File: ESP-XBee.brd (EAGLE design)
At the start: 10 parts, among them SW1 434111043826

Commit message: seeedstudio GERBER generated
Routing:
- net N$2: track 109.9 -> 0.00 mm
- net RESET: track 45.6 -> 47.1 mm, vias 3 -> 2
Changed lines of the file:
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@@
 </class>
 </classes>
-<designrules name="default">
+<designrules name="SeeedStudio_2layer_DRU_no_angle_20140221">
 <description language="de">&lt;b&gt;EAGLE Design Rules&lt;/b&gt;
 &lt;p&gt;
@@
 necessary adjustments and save your customized
 design rules under a new name.</description>
+<description language="zh">&lt;b&gt;Seeed Studio EAGLE Design Rules&lt;/b&gt;
+</description>
 <param name="layerSetup" value="(1*16)"/>
-<param name="mtCopper" value="0.035mm 0.035mm 0.035mm 0.035mm 0.035mm 0.035mm 0.035mm 0.035mm 0.035mm 0.035mm 0.035mm 0.035mm 0.035mm 0.035mm 0.035mm 0.035mm"/>
-<param name="mtIsolate" value="1.5mm 0.15mm 0.2mm 0.15mm 0.2mm 0.15mm 0.2mm 0.15mm 0.2mm 0.15mm 0.2mm 0.15mm 0.2mm 0.15mm 0.2mm"/>
-<param name="mdWireWire" value="8mil"/>
-<param name="mdWirePad" value="8mil"/>
-<param name="mdWireVia" value="8mil"/>
-<param name="mdPadPad" value="8mil"/>
-<param name="mdPadVia" value="8mil"/>
-<param name="mdViaVia" value="8mil"/>
-<param name="mdSmdPad" value="8mil"/>
-<param name="mdSmdVia" value="8mil"/>
-<param name="mdSmdSmd" value="8mil"/>
+<param name="mtCopper" value="0.035mm 0.0175mm 0.035mm 0.035mm 0.035mm 0.035mm 0.035mm 0.035mm 0.035mm 0.035mm 0.035mm 0.035mm 0.035mm 0.035mm 0.0175mm 0.035mm"/>
+<param name="mtIsolate" value="1.5mm 1.1mm 0.2mm 0.15mm 0.2mm 0.15mm 0.2mm 0.15mm 0.2mm 0.15mm 0.2mm 0.15mm 0.2mm 0.15mm 0.2mm"/>
+<param name="mdWireWire" value="6mil"/>
+<param name="mdWirePad" value="6mil"/>
+<param name="mdWireVia" value="6mil"/>
+<param name="mdPadPad" value="6mil"/>
+<param name="mdPadVia" value="6mil"/>
+<param name="mdViaVia" value="6mil"/>
+<param name="mdSmdPad" value="0mil"/>
+<param name="mdSmdVia" value="0mil"/>
+<param name="mdSmdSmd" value="0mil"/>
 <param name="mdViaViaSameLayer" value="8mil"/>
 <param name="mnLayersViaInSmd" value="2"/>
-<param name="mdCopperDimension" value="40mil"/>
-<param name="mdDrill" value="8mil"/>
+<param name="mdCopperDimension" value="10mil"/>
+<param name="mdDrill" value="10mil"/>
 <param name="mdSmdStop" value="0mil"/>
-<param name="msWidth" value="10mil"/>
-<param name="msDrill" value="24mil"/>
-<param name="msMicroVia" value="9.99mm"/>
+<param name="msWidth" value="6mil"/>
+<param name="msDrill" value="12mil"/>
+<param name="msMicroVia" value="12mil"/>
 <param name="msBlindViaRatio" value="0.5"/>
 <param name="rvPadTop" value="0.25"/>
@@
 <param name="rlMinPadBottom" value="10mil"/>
 <param name="rlMaxPadBottom" value="20mil"/>
-<param name="rlMinViaOuter" value="8mil"/>
+<param name="rlMinViaOuter" value="6mil"/>
 <param name="rlMaxViaOuter" value="20mil"/>
-<param name="rlMinViaInner" value="8mil"/>
+<param name="rlMinViaInner" value="6mil"/>
 <param name="rlMaxViaInner" value="20mil"/>
 <param name="rlMinMicroViaOuter" value="4mil"/>
@@
 <param name="psTop" value="-1"/>
 <param name="psBottom" value="-1"/>
-<param name="psFirst" value="-1"/>
+<param name="psFirst" value="0"/>
 <param name="psElongationLong" value="100"/>
 <param name="psElongationOffset" value="100"/>
 <param name="mvStopFrame" value="1"/>
 <param name="mvCreamFrame" value="0"/>
-<param name="mlMinStopFrame" value="4mil"/>
-<param name="mlMaxStopFrame" value="4mil"/>
+<param name="mlMinStopFrame" value="2mil"/>
+<param name="mlMaxStopFrame" value="2mil"/>
 <param name="mlMinCreamFrame" value="0mil"/>
 <param name="mlMaxCreamFrame" value="0mil"/>
-<param name="mlViaStopLimit" value="0mil"/>
+<param name="mlViaStopLimit" value="100mil"/>
 <param name="srRoundness" value="0"/>
 <param name="srMinRoundness" value="0mil"/>
@@
 <param name="checkAngle" value="0"/>
 <param name="checkFont" value="1"/>
-<param name="checkRestrict" value="1"/>
+<param name="checkRestrict" value="0"/>
 <param name="useDiameter" value="13"/>
 <param name="maxErrors" value="50"/>
@@
 <contactref element="C2" pad="1"/>
 <contactref element="R5" pad="2"/>
-<wire x1="34.417" y1="42.543" x2="36.197" y2="42.543" width="0.3048" layer="1"/>
-<wire x1="36.197" y1="42.543" x2="36.83" y2="41.91" width="0.3048" layer="1"/>
-<via x="36.83" y="41.91" extent="1-16" drill="0.6" shape="octagon"/>
-<wire x1="36.83" y1="41.91" x2="36.83" y2="40.64" width="0.3048" layer="16"/>
-<wire x1="36.83" y1="40.64" x2="36.195" y2="40.005" width="0.3048" layer="16"/>
-<wire x1="36.195" y1="40.005" x2="34.798" y2="40.005" width="0.3048" layer="16"/>
-<wire x1="34.798" y1="40.005" x2="34.417" y2="39.624" width="0.3048" layer="16"/>
-<wire x1="34.417" y1="39.624" x2="34.417" y2="38.481" width="0.3048" layer="16"/>
-<wire x1="34.417" y1="38.481" x2="33.274" y2="37.338" width="0.3048" layer="16"/>
-<wire x1="33.274" y1="37.338" x2="31.607" y2="37.338" width="0.3048" layer="16"/>
-<wire x1="31.607" y1="37.338" x2="31.545" y2="37.4" width="0.3048" layer="16"/>
 <wire x1="42.407" y1="22.225" x2="42.407" y2="23.357" width="0.3048" layer="1"/>
 <wire x1="42.407" y1="23.357" x2="43.18" y2="24.13" width="0.3048" layer="1"/>
@@
 <wire x1="46.101" y1="32.131" x2="45.201" y2="32.131" width="0.3048" layer="16"/>
 <wire x1="45.201" y1="32.131" x2="44.958" y2="31.38" width="0.3048" layer="16"/>
-<wire x1="36.83" y1="40.64" x2="36.83" y2="40.513" width="0.3048" layer="16"/>
-<wire x1="36.83" y1="40.513" x2="39.243" y2="36.83" width="0.3048" layer="16"/>
-<via x="39.243" y="36.83" extent="1-16" drill="0.6" shape="octagon"/>
-<wire x1="39.243" y1="36.83" x2="43.688" y2="36.83" width="0.3048" layer="1"/>
 <wire x1="43.688" y1="36.83" x2="46.101" y2="34.417" width="0.3048" layer="1"/>
 <wire x1="46.101" y1="34.417" x2="46.101" y2="32.131" width="0.3048" layer="1"/>
+<wire x1="43.688" y1="36.83" x2="40.005" y2="36.83" width="0.3048" layer="1"/>
+<wire x1="40.005" y1="36.83" x2="39.243" y2="37.592" width="0.3048" layer="1"/>
+<wire x1="39.243" y1="37.592" x2="39.243" y2="40.64" width="0.3048" layer="1"/>
+<wire x1="31.545" y1="37.4" x2="32.955" y2="37.4" width="0.3048" layer="16"/>
+<wire x1="32.955" y1="37.4" x2="36.83" y2="41.275" width="0.3048" layer="16"/>
+<wire x1="34.542" y1="42.418" x2="34.417" y2="42.543" width="0.3048" layer="1"/>
+<wire x1="36.83" y1="41.275" x2="36.83" y2="42.545" width="0.3048" layer="16"/>
+<via x="36.83" y="42.545" extent="1-16" drill="0.6" shape="octagon"/>
+<wire x1="36.83" y1="42.545" x2="34.419" y2="42.545" width="0.3048" layer="1"/>
+<wire x1="34.419" y1="42.545" x2="34.417" y2="42.543" width="0.3048" layer="1"/>
+<wire x1="39.243" y1="40.64" x2="37.338" y2="42.545" width="0.3048" layer="1"/>
+<wire x1="37.338" y1="42.545" x2="36.83" y2="42.545" width="0.3048" layer="1"/>
 </signal>
 <signal name="ADC">
@@
 <wire x1="46.18" y1="22.225" x2="44.207" y2="22.225" width="0.3048" layer="1"/>
 </signal>
-<signal name="N$2">
-<wire x1="30.48" y1="19.05" x2="55.245" y2="19.05" width="0.4064" layer="16"/>
-<wire x1="55.245" y1="19.05" x2="55.245" y2="46.355" width="0.4064" layer="16"/>
-<wire x1="55.245" y1="46.355" x2="47.625" y2="53.34" width="0.4064" layer="16"/>
-<wire x1="47.625" y1="53.34" x2="37.465" y2="53.34" width="0.4064" layer="16"/>
-<wire x1="30.48" y1="46.99" x2="30.48" y2="19.05" width="0.4064" layer="16"/>
-<wire x1="30.48" y1="46.99" x2="37.465" y2="53.213" width="0.3048" layer="16"/>
-</signal>
 </signals>

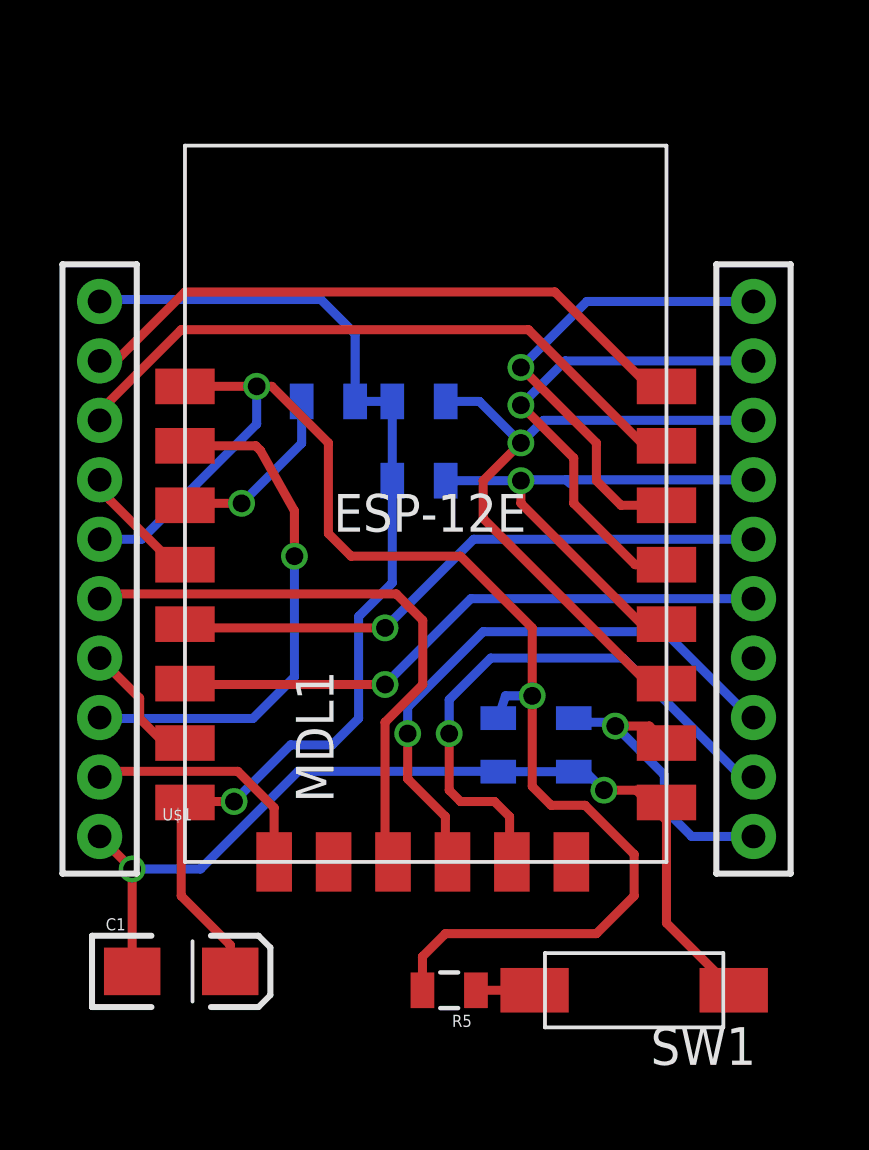
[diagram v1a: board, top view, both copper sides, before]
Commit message: Revert "seeedstudio GERBER generated"
This reverts commit 3978db2b9afe7cefcf6061ea9ca2f2ffcfdcaa63.
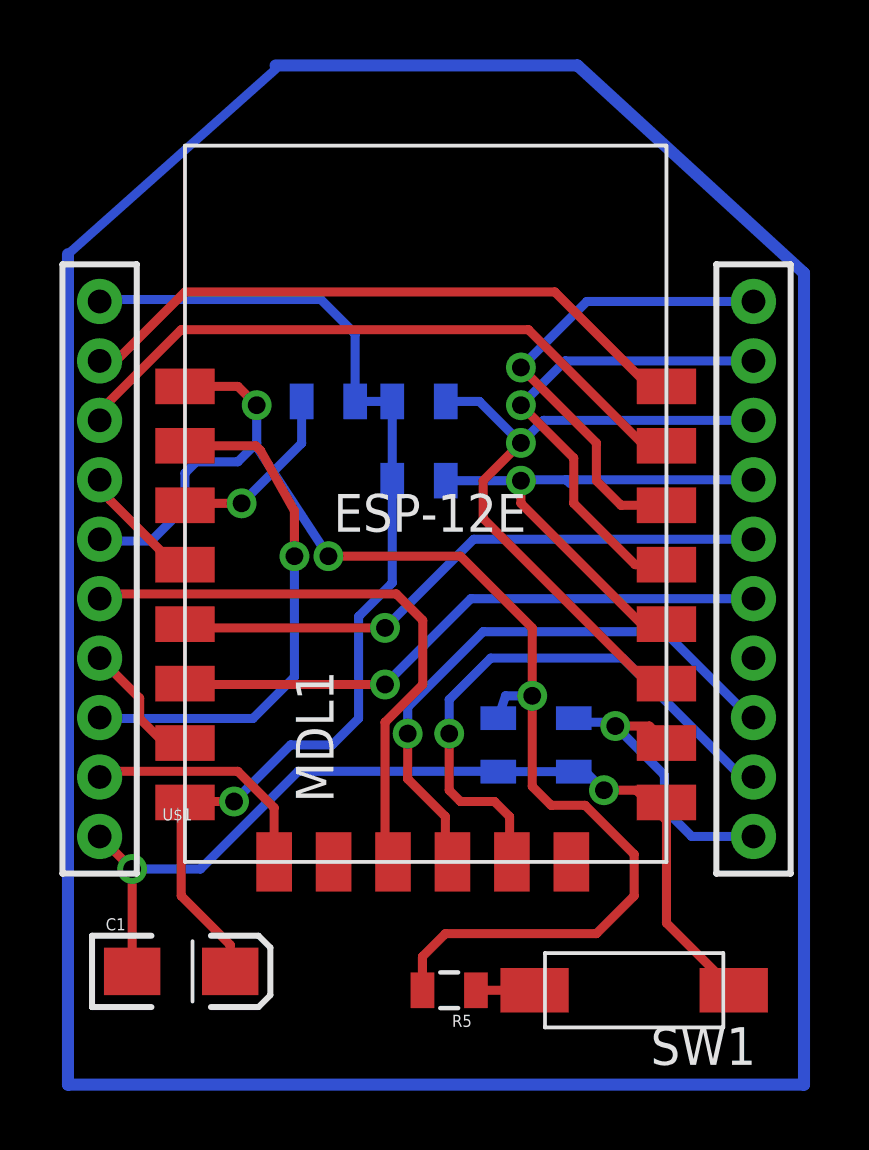
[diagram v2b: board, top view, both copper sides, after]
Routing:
- net N$2: track 0.00 -> 109.9 mm
- net RESET: track 47.1 -> 45.6 mm, vias 2 -> 3
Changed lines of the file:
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@@
 </class>
 </classes>
-<designrules name="SeeedStudio_2layer_DRU_no_angle_20140221">
+<designrules name="default">
 <description language="de">&lt;b&gt;EAGLE Design Rules&lt;/b&gt;
 &lt;p&gt;
@@
 necessary adjustments and save your customized
 design rules under a new name.</description>
-<description language="zh">&lt;b&gt;Seeed Studio EAGLE Design Rules&lt;/b&gt;
-</description>
 <param name="layerSetup" value="(1*16)"/>
-<param name="mtCopper" value="0.035mm 0.0175mm 0.035mm 0.035mm 0.035mm 0.035mm 0.035mm 0.035mm 0.035mm 0.035mm 0.035mm 0.035mm 0.035mm 0.035mm 0.0175mm 0.035mm"/>
-<param name="mtIsolate" value="1.5mm 1.1mm 0.2mm 0.15mm 0.2mm 0.15mm 0.2mm 0.15mm 0.2mm 0.15mm 0.2mm 0.15mm 0.2mm 0.15mm 0.2mm"/>
-<param name="mdWireWire" value="6mil"/>
-<param name="mdWirePad" value="6mil"/>
-<param name="mdWireVia" value="6mil"/>
-<param name="mdPadPad" value="6mil"/>
-<param name="mdPadVia" value="6mil"/>
-<param name="mdViaVia" value="6mil"/>
-<param name="mdSmdPad" value="0mil"/>
-<param name="mdSmdVia" value="0mil"/>
-<param name="mdSmdSmd" value="0mil"/>
+<param name="mtCopper" value="0.035mm 0.035mm 0.035mm 0.035mm 0.035mm 0.035mm 0.035mm 0.035mm 0.035mm 0.035mm 0.035mm 0.035mm 0.035mm 0.035mm 0.035mm 0.035mm"/>
+<param name="mtIsolate" value="1.5mm 0.15mm 0.2mm 0.15mm 0.2mm 0.15mm 0.2mm 0.15mm 0.2mm 0.15mm 0.2mm 0.15mm 0.2mm 0.15mm 0.2mm"/>
+<param name="mdWireWire" value="8mil"/>
+<param name="mdWirePad" value="8mil"/>
+<param name="mdWireVia" value="8mil"/>
+<param name="mdPadPad" value="8mil"/>
+<param name="mdPadVia" value="8mil"/>
+<param name="mdViaVia" value="8mil"/>
+<param name="mdSmdPad" value="8mil"/>
+<param name="mdSmdVia" value="8mil"/>
+<param name="mdSmdSmd" value="8mil"/>
 <param name="mdViaViaSameLayer" value="8mil"/>
 <param name="mnLayersViaInSmd" value="2"/>
-<param name="mdCopperDimension" value="10mil"/>
-<param name="mdDrill" value="10mil"/>
+<param name="mdCopperDimension" value="40mil"/>
+<param name="mdDrill" value="8mil"/>
 <param name="mdSmdStop" value="0mil"/>
-<param name="msWidth" value="6mil"/>
-<param name="msDrill" value="12mil"/>
-<param name="msMicroVia" value="12mil"/>
+<param name="msWidth" value="10mil"/>
+<param name="msDrill" value="24mil"/>
+<param name="msMicroVia" value="9.99mm"/>
 <param name="msBlindViaRatio" value="0.5"/>
 <param name="rvPadTop" value="0.25"/>
@@
 <param name="rlMinPadBottom" value="10mil"/>
 <param name="rlMaxPadBottom" value="20mil"/>
-<param name="rlMinViaOuter" value="6mil"/>
+<param name="rlMinViaOuter" value="8mil"/>
 <param name="rlMaxViaOuter" value="20mil"/>
-<param name="rlMinViaInner" value="6mil"/>
+<param name="rlMinViaInner" value="8mil"/>
 <param name="rlMaxViaInner" value="20mil"/>
 <param name="rlMinMicroViaOuter" value="4mil"/>
@@
 <param name="psTop" value="-1"/>
 <param name="psBottom" value="-1"/>
-<param name="psFirst" value="0"/>
+<param name="psFirst" value="-1"/>
 <param name="psElongationLong" value="100"/>
 <param name="psElongationOffset" value="100"/>
 <param name="mvStopFrame" value="1"/>
 <param name="mvCreamFrame" value="0"/>
-<param name="mlMinStopFrame" value="2mil"/>
-<param name="mlMaxStopFrame" value="2mil"/>
+<param name="mlMinStopFrame" value="4mil"/>
+<param name="mlMaxStopFrame" value="4mil"/>
 <param name="mlMinCreamFrame" value="0mil"/>
 <param name="mlMaxCreamFrame" value="0mil"/>
-<param name="mlViaStopLimit" value="100mil"/>
+<param name="mlViaStopLimit" value="0mil"/>
 <param name="srRoundness" value="0"/>
 <param name="srMinRoundness" value="0mil"/>
@@
 <param name="checkAngle" value="0"/>
 <param name="checkFont" value="1"/>
-<param name="checkRestrict" value="0"/>
+<param name="checkRestrict" value="1"/>
 <param name="useDiameter" value="13"/>
 <param name="maxErrors" value="50"/>
@@
 <contactref element="C2" pad="1"/>
 <contactref element="R5" pad="2"/>
+<wire x1="34.417" y1="42.543" x2="36.197" y2="42.543" width="0.3048" layer="1"/>
+<wire x1="36.197" y1="42.543" x2="36.83" y2="41.91" width="0.3048" layer="1"/>
+<via x="36.83" y="41.91" extent="1-16" drill="0.6" shape="octagon"/>
+<wire x1="36.83" y1="41.91" x2="36.83" y2="40.64" width="0.3048" layer="16"/>
+<wire x1="36.83" y1="40.64" x2="36.195" y2="40.005" width="0.3048" layer="16"/>
+<wire x1="36.195" y1="40.005" x2="34.798" y2="40.005" width="0.3048" layer="16"/>
+<wire x1="34.798" y1="40.005" x2="34.417" y2="39.624" width="0.3048" layer="16"/>
+<wire x1="34.417" y1="39.624" x2="34.417" y2="38.481" width="0.3048" layer="16"/>
+<wire x1="34.417" y1="38.481" x2="33.274" y2="37.338" width="0.3048" layer="16"/>
+<wire x1="33.274" y1="37.338" x2="31.607" y2="37.338" width="0.3048" layer="16"/>
+<wire x1="31.607" y1="37.338" x2="31.545" y2="37.4" width="0.3048" layer="16"/>
 <wire x1="42.407" y1="22.225" x2="42.407" y2="23.357" width="0.3048" layer="1"/>
 <wire x1="42.407" y1="23.357" x2="43.18" y2="24.13" width="0.3048" layer="1"/>
@@
 <wire x1="46.101" y1="32.131" x2="45.201" y2="32.131" width="0.3048" layer="16"/>
 <wire x1="45.201" y1="32.131" x2="44.958" y2="31.38" width="0.3048" layer="16"/>
+<wire x1="36.83" y1="40.64" x2="36.83" y2="40.513" width="0.3048" layer="16"/>
+<wire x1="36.83" y1="40.513" x2="39.243" y2="36.83" width="0.3048" layer="16"/>
+<via x="39.243" y="36.83" extent="1-16" drill="0.6" shape="octagon"/>
+<wire x1="39.243" y1="36.83" x2="43.688" y2="36.83" width="0.3048" layer="1"/>
 <wire x1="43.688" y1="36.83" x2="46.101" y2="34.417" width="0.3048" layer="1"/>
 <wire x1="46.101" y1="34.417" x2="46.101" y2="32.131" width="0.3048" layer="1"/>
-<wire x1="43.688" y1="36.83" x2="40.005" y2="36.83" width="0.3048" layer="1"/>
-<wire x1="40.005" y1="36.83" x2="39.243" y2="37.592" width="0.3048" layer="1"/>
-<wire x1="39.243" y1="37.592" x2="39.243" y2="40.64" width="0.3048" layer="1"/>
-<wire x1="31.545" y1="37.4" x2="32.955" y2="37.4" width="0.3048" layer="16"/>
-<wire x1="32.955" y1="37.4" x2="36.83" y2="41.275" width="0.3048" layer="16"/>
-<wire x1="34.542" y1="42.418" x2="34.417" y2="42.543" width="0.3048" layer="1"/>
-<wire x1="36.83" y1="41.275" x2="36.83" y2="42.545" width="0.3048" layer="16"/>
-<via x="36.83" y="42.545" extent="1-16" drill="0.6" shape="octagon"/>
-<wire x1="36.83" y1="42.545" x2="34.419" y2="42.545" width="0.3048" layer="1"/>
-<wire x1="34.419" y1="42.545" x2="34.417" y2="42.543" width="0.3048" layer="1"/>
-<wire x1="39.243" y1="40.64" x2="37.338" y2="42.545" width="0.3048" layer="1"/>
-<wire x1="37.338" y1="42.545" x2="36.83" y2="42.545" width="0.3048" layer="1"/>
 </signal>
 <signal name="ADC">
@@
 <wire x1="46.18" y1="22.225" x2="44.207" y2="22.225" width="0.3048" layer="1"/>
 </signal>
+<signal name="N$2">
+<wire x1="30.48" y1="19.05" x2="55.245" y2="19.05" width="0.4064" layer="16"/>
+<wire x1="55.245" y1="19.05" x2="55.245" y2="46.355" width="0.4064" layer="16"/>
+<wire x1="55.245" y1="46.355" x2="47.625" y2="53.34" width="0.4064" layer="16"/>
+<wire x1="47.625" y1="53.34" x2="37.465" y2="53.34" width="0.4064" layer="16"/>
+<wire x1="30.48" y1="46.99" x2="30.48" y2="19.05" width="0.4064" layer="16"/>
+<wire x1="30.48" y1="46.99" x2="37.465" y2="53.213" width="0.3048" layer="16"/>
+</signal>
 </signals>
